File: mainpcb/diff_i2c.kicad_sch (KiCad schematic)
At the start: 24 parts, among them J4 Conn_01x08, J5 Conn_01x03, J6 Conn_01x08, J7 Conn_01x03, U1 PCA9615DP, U6 PCA9615DP

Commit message: Added limit switches to hand and readme
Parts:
- removed J7: Conn_01x03, Connector_PinHeader_2.54mm:PinHeader_1x03_P2.54mm_Vertical, symbol Connector_Generic:Conn_01x03
- removed R12, R13: 10kR, symbol Device:R_US
- C10: renamed from C14; footprint Capacitor_THT:C_Disc_D8.0mm_W2.5mm_P5.00mm -> Capacitor_THT:C_Rect_L4.6mm_W2.0mm_P2.50mm_MKS02_FKP02
- C9: renamed from C13; footprint Capacitor_THT:C_Disc_D8.0mm_W2.5mm_P5.00mm -> Capacitor_THT:C_Rect_L4.6mm_W2.0mm_P2.50mm_MKS02_FKP02
- R10: renamed from R5; footprint (none) -> Resistor_THT:R_Axial_DIN0207_L6.3mm_D2.5mm_P10.16mm_Horizontal
- R11: renamed from R6; footprint (none) -> Resistor_THT:R_Axial_DIN0207_L6.3mm_D2.5mm_P10.16mm_Horizontal
- R12: renamed from R14; footprint (none) -> Resistor_THT:R_Axial_DIN0207_L6.3mm_D2.5mm_P10.16mm_Horizontal
- R13: renamed from R7; footprint (none) -> Resistor_THT:R_Axial_DIN0207_L6.3mm_D2.5mm_P10.16mm_Horizontal
- R14: renamed from R15; footprint (none) -> Resistor_THT:R_Axial_DIN0207_L6.3mm_D2.5mm_P10.16mm_Horizontal
- R15: renamed from R8; footprint (none) -> Resistor_THT:R_Axial_DIN0207_L6.3mm_D2.5mm_P10.16mm_Horizontal
- R16: footprint (none) -> Resistor_THT:R_Axial_DIN0207_L6.3mm_D2.5mm_P10.16mm_Horizontal
- R3: renamed from R1; footprint (none) -> Resistor_THT:R_Axial_DIN0207_L6.3mm_D2.5mm_P10.16mm_Horizontal
- R4: renamed from R9; footprint (none) -> Resistor_THT:R_Axial_DIN0207_L6.3mm_D2.5mm_P10.16mm_Horizontal
- R5: renamed from R2; footprint (none) -> Resistor_THT:R_Axial_DIN0207_L6.3mm_D2.5mm_P10.16mm_Horizontal
- R6: renamed from R10; footprint (none) -> Resistor_THT:R_Axial_DIN0207_L6.3mm_D2.5mm_P10.16mm_Horizontal
- R7: renamed from R3; footprint (none) -> Resistor_THT:R_Axial_DIN0207_L6.3mm_D2.5mm_P10.16mm_Horizontal
- R8: renamed from R11; footprint (none) -> Resistor_THT:R_Axial_DIN0207_L6.3mm_D2.5mm_P10.16mm_Horizontal
- R9: renamed from R4; footprint (none) -> Resistor_THT:R_Axial_DIN0207_L6.3mm_D2.5mm_P10.16mm_Horizontal
- renumbered J4 to J6, J6 to J7, J5 to J8, U1 to U5

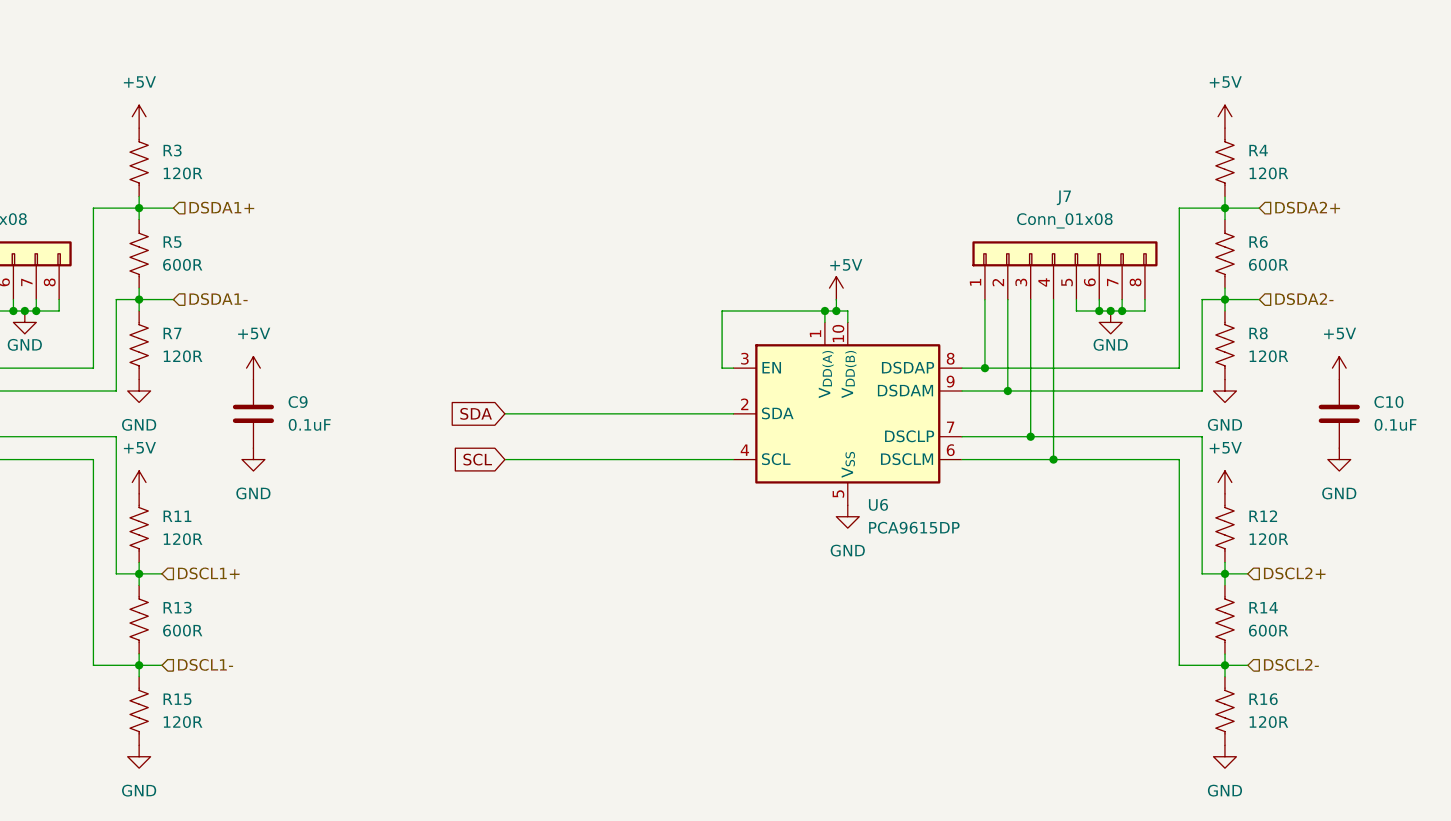
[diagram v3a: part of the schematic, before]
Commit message: Version 1 AS-BUILT commit
This commit has the schematics of version 1 of the system AS IT WAS BUILT
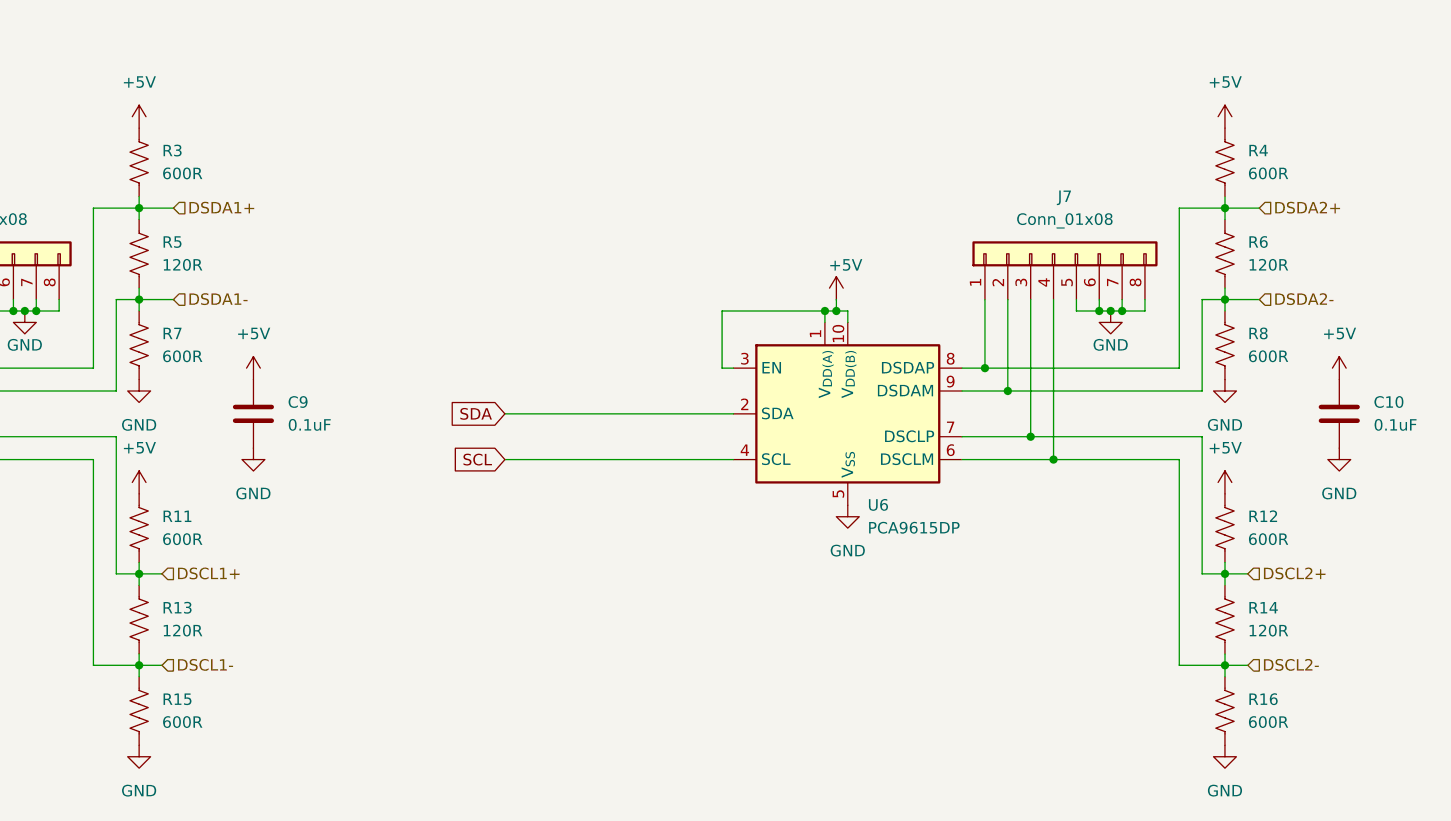
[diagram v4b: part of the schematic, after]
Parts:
- R11, R12, R15, R16, R3, R4, R7, R8: value 120R -> 600R
- R13, R14, R5, R6: value 600R -> 120R
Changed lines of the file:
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@@
 			)
 		)
-		(property "Value" "120R"
+		(property "Value" "600R"
 			(at 236.22 105.4099 0)
 			(effects
@@
 			)
 		)
-		(property "Value" "600R"
+		(property "Value" "120R"
 			(at 115.57 74.9299 0)
 			(effects
@@
 			)
 		)
-		(property "Value" "120R"
+		(property "Value" "600R"
 			(at 115.57 105.4099 0)
 			(effects
@@
 			)
 		)
-		(property "Value" "120R"
+		(property "Value" "600R"
 			(at 115.57 64.7699 0)
 			(effects
@@
 			)
 		)
-		(property "Value" "600R"
+		(property "Value" "120R"
 			(at 236.22 115.5699 0)
 			(effects
@@
 			)
 		)
-		(property "Value" "120R"
+		(property "Value" "600R"
 			(at 236.22 85.0899 0)
 			(effects
@@
 			)
 		)
-		(property "Value" "600R"
+		(property "Value" "120R"
 			(at 115.57 115.5699 0)
 			(effects
@@
 			)
 		)
-		(property "Value" "120R"
+		(property "Value" "600R"
 			(at 115.57 125.7299 0)
 			(effects
@@
 			)
 		)
-		(property "Value" "600R"
+		(property "Value" "120R"
 			(at 236.22 74.9299 0)
 			(effects
@@
 			)
 		)
-		(property "Value" "120R"
+		(property "Value" "600R"
 			(at 236.22 125.7299 0)
 			(effects
@@
 			)
 		)
-		(property "Value" "120R"
+		(property "Value" "600R"
 			(at 115.57 85.0899 0)
 			(effects
@@
 			)
 		)
-		(property "Value" "120R"
+		(property "Value" "600R"
 			(at 236.22 64.7699 0)
 			(effects

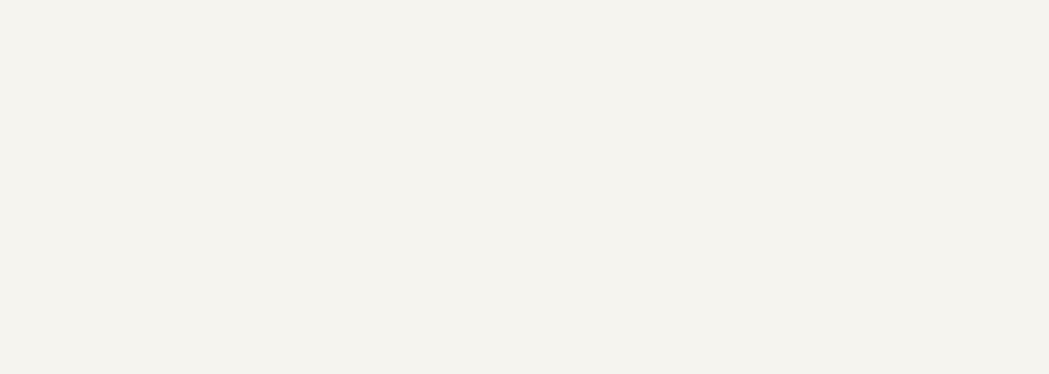
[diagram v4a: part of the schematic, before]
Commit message: Added drawing information boxes
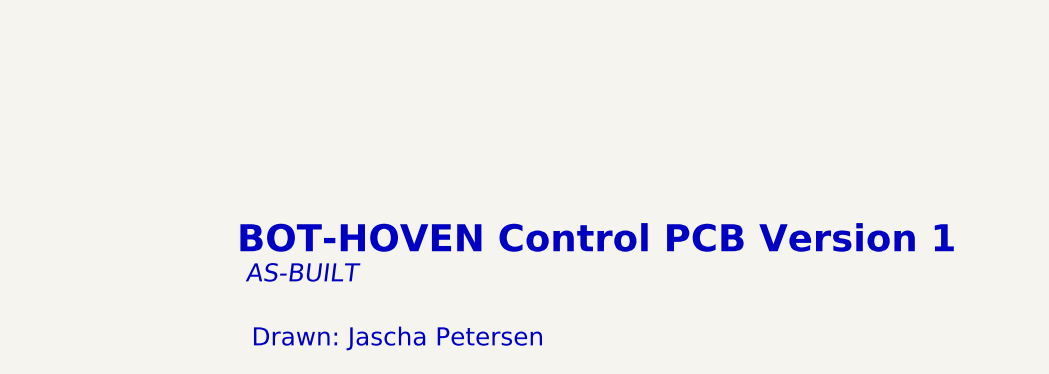
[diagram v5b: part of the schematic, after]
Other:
- note added: "AS-BUILT"
- note added: "BOT-HOVEN Control PCB Version 1"
- note added: "Drawn: Jascha Petersen"
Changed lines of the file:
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@@
+		)
+	)
+	(text "AS-BUILT"
+		(exclude_from_sim no)
+		(at 184.912 172.974 0)
+		(effects
+			(font
+				(size 2 2)
+				(italic yes)
+			)
+		)
+	)
+	(text "BOT-HOVEN Control PCB Version 1"
+		(exclude_from_sim no)
+		(at 217.678 169.164 0)
+		(effects
+			(font
+				(size 3 3)
+				(thickness 0.6)
+				(bold yes)
+			)
+		)
+	)
+	(text "Drawn: Jascha Petersen"
+		(exclude_from_sim no)
+		(at 195.58 180.086 0)
+		(effects
+			(font
+				(size 2 2)
+			)
 		)
 	)

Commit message: Added PDF schematic exports
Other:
- title: (none) -> Control PCB Differential I2C
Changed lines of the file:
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@@
 	(generator_version "8.0")
 	(paper "A4")
+	(title_block
+		(title "Control PCB Differential I2C")
+	)
 	(junction
 		(at 113.03 78.74)
